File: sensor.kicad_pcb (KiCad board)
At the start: 2 copper layers, 18.4 x 42 mm, 13 parts, among them J1 Conn_01x06_Female, U2 TLV70019_SOT23-5, U3 TXB0106PWR, U4 PMW3360DM-T2QU

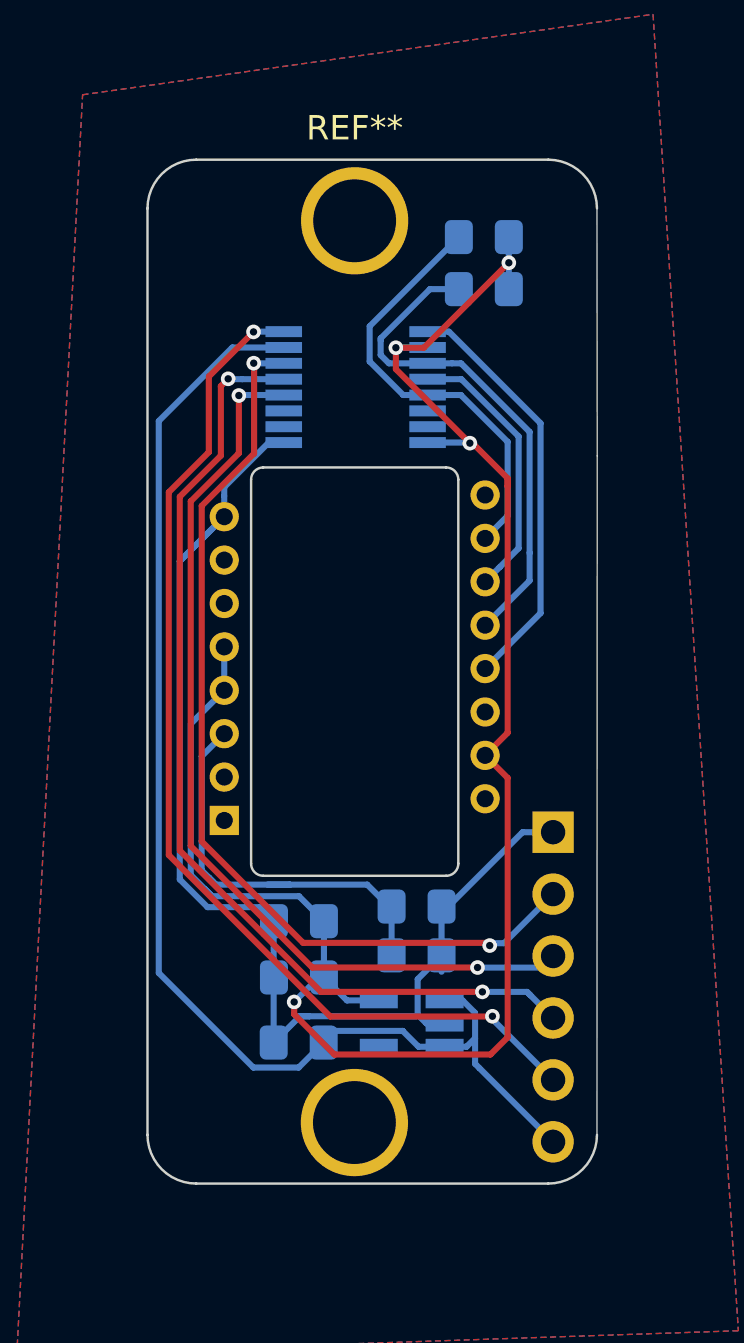
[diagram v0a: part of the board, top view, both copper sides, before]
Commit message: slightly bigger edge cuts for M3 holes
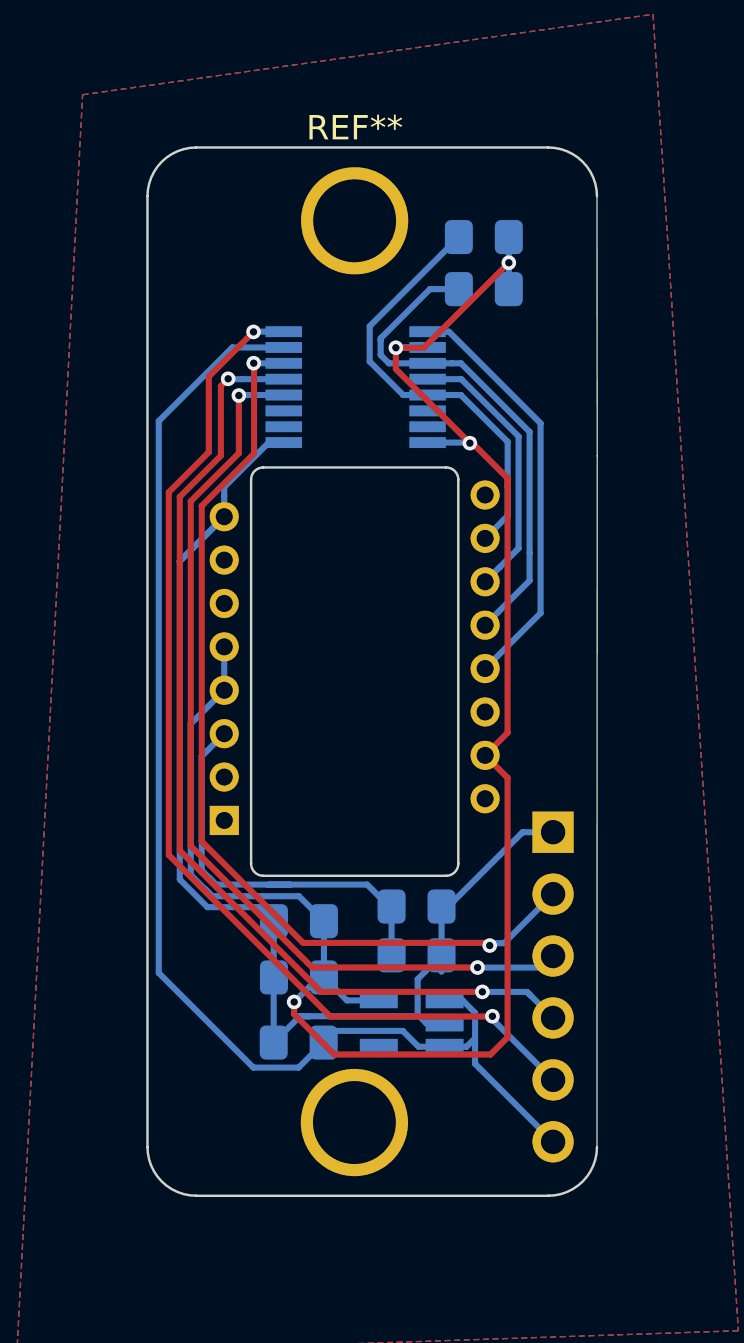
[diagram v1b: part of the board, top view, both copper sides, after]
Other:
- board size 18.4 x 42 mm -> 18.4 x 43 mm
- board text added: "rev 1.1"
- board text removed: "rev 1.0"
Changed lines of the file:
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@@
       (viasonmask false)
       (mode 1)
-      (useauxorigin false)
+      (useauxorigin true)
       (hpglpennumber 1)
       (hpglpenspeed 20)
@@
       (drillshape 0)
       (scaleselection 1)
-      (outputdirectory "../gerber/sensorPcb/")
+      (outputdirectory "gerber/")
     )
   )
@@
     (fp_line (start 1 -0.6) (end -1 -0.6) (layer "B.Fab") (width 0.1))
     (fp_line (start -1 -0.6) (end -1 0.6) (layer "B.Fab") (width 0.1))
-    (pad "1" smd roundrect (at -1.025 0) (locked) (size 1.15 1.4) (layers "B.Cu" "B.Paste" "B.Mask") (roundrect_rratio 0.217391)
+    (pad "1" smd roundrect (at -1.025 0) (locked) (size 1.15 1.4) (layers "B.Cu" "B.Paste" "B.Mask") (roundrect_rratio 0.2173913043478261)
       (net 12 "MISO") (pintype "passive"))
-    (pad "2" smd roundrect (at 1.025 0) (locked) (size 1.15 1.4) (layers "B.Cu" "B.Paste" "B.Mask") (roundrect_rratio 0.217391)
+    (pad "2" smd roundrect (at 1.025 0) (locked) (size 1.15 1.4) (layers "B.Cu" "B.Paste" "B.Mask") (roundrect_rratio 0.2173913043478261)
       (net 3 "VDD_1.9V") (pintype "passive"))
     (model "${KISYS3DMOD}/Resistor_SMD.3dshapes/R_0805_2012Metric.wrl"
@@
     (fp_line (start -1 0.6) (end 1 0.6) (layer "B.Fab") (width 0.1))
     (fp_line (start 1 0.6) (end 1 -0.6) (layer "B.Fab") (width 0.1))
-    (pad "1" smd roundrect (at -1.025 0) (locked) (size 1.15 1.4) (layers "B.Cu" "B.Paste" "B.Mask") (roundrect_rratio 0.217391)
+    (pad "1" smd roundrect (at -1.025 0) (locked) (size 1.15 1.4) (layers "B.Cu" "B.Paste" "B.Mask") (roundrect_rratio 0.2173913043478261)
       (net 10 "SCLK") (pintype "passive"))
-    (pad "2" smd roundrect (at 1.025 0) (locked) (size 1.15 1.4) (layers "B.Cu" "B.Paste" "B.Mask") (roundrect_rratio 0.217391)
+    (pad "2" smd roundrect (at 1.025 0) (locked) (size 1.15 1.4) (layers "B.Cu" "B.Paste" "B.Mask") (roundrect_rratio 0.2173913043478261)
       (net 3 "VDD_1.9V") (pintype "passive"))
     (model "${KISYS3DMOD}/Resistor_SMD.3dshapes/R_0805_2012Metric.wrl"
@@
     (fp_line (start 1 0.6) (end 1 -0.6) (layer "B.Fab") (width 0.1))
     (fp_line (start -1 0.6) (end 1 0.6) (layer "B.Fab") (width 0.1))
-    (pad "1" smd roundrect (at -1.025 0 180) (locked) (size 1.15 1.4) (layers "B.Cu" "B.Paste" "B.Mask") (roundrect_rratio 0.217391)
+    (pad "1" smd roundrect (at -1.025 0 180) (locked) (size 1.15 1.4) (layers "B.Cu" "B.Paste" "B.Mask") (roundrect_rratio 0.2173913043478261)
       (net 3 "VDD_1.9V") (pintype "passive"))
-    (pad "2" smd roundrect (at 1.025 0 180) (locked) (size 1.15 1.4) (layers "B.Cu" "B.Paste" "B.Mask") (roundrect_rratio 0.217391)
+    (pad "2" smd roundrect (at 1.025 0 180) (locked) (size 1.15 1.4) (layers "B.Cu" "B.Paste" "B.Mask") (roundrect_rratio 0.2173913043478261)
       (net 1 "GND") (pintype "passive"))
     (model "${KISYS3DMOD}/Capacitor_SMD.3dshapes/C_0805_2012Metric.wrl"
@@
     (fp_line (start 1 0.6) (end 1 -0.6) (layer "B.Fab") (width 0.1))
     (fp_line (start -1 -0.6) (end -1 0.6) (layer "B.Fab") (width 0.1))
-    (pad "1" smd roundrect (at -1.025 0 180) (locked) (size 1.15 1.4) (layers "B.Cu" "B.Paste" "B.Mask") (roundrect_rratio 0.217391)
+    (pad "1" smd roundrect (at -1.025 0 180) (locked) (size 1.15 1.4) (layers "B.Cu" "B.Paste" "B.Mask") (roundrect_rratio 0.2173913043478261)
       (net 2 "VDD_5V") (pintype "passive"))
-    (pad "2" smd roundrect (at 1.025 0 180) (locked) (size 1.15 1.4) (layers "B.Cu" "B.Paste" "B.Mask") (roundrect_rratio 0.217391)
+    (pad "2" smd roundrect (at 1.025 0 180) (locked) (size 1.15 1.4) (layers "B.Cu" "B.Paste" "B.Mask") (roundrect_rratio 0.2173913043478261)
       (net 1 "GND") (pintype "passive"))
     (model "${KISYS3DMOD}/Capacitor_SMD.3dshapes/C_0805_2012Metric.wrl"
@@
     (fp_line (start -1 -0.6) (end -1 0.6) (layer "B.Fab") (width 0.1))
     (fp_line (start 1 0.6) (end 1 -0.6) (layer "B.Fab") (width 0.1))
-    (pad "1" smd roundrect (at -1.025 0) (locked) (size 1.15 1.4) (layers "B.Cu" "B.Paste" "B.Mask") (roundrect_rratio 0.217391)
+    (pad "1" smd roundrect (at -1.025 0) (locked) (size 1.15 1.4) (layers "B.Cu" "B.Paste" "B.Mask") (roundrect_rratio 0.2173913043478261)
       (net 4 "Net-(C3-Pad1)"))
-    (pad "2" smd roundrect (at 1.025 0) (locked) (size 1.15 1.4) (layers "B.Cu" "B.Paste" "B.Mask") (roundrect_rratio 0.217391)
+    (pad "2" smd roundrect (at 1.025 0) (locked) (size 1.15 1.4) (layers "B.Cu" "B.Paste" "B.Mask") (roundrect_rratio 0.2173913043478261)
       (net 1 "GND"))
     (model "${KISYS3DMOD}/Capacitor_SMD.3dshapes/C_0805_2012Metric.wrl"
@@
     (fp_line (start 1 -0.6) (end -1 -0.6) (layer "B.Fab") (width 0.1))
     (fp_line (start -1 -0.6) (end -1 0.6) (layer "B.Fab") (width 0.1))
-    (pad "1" smd roundrect (at -1.025 0 180) (locked) (size 1.15 1.4) (layers "B.Cu" "B.Paste" "B.Mask") (roundrect_rratio 0.217391)
+    (pad "1" smd roundrect (at -1.025 0 180) (locked) (size 1.15 1.4) (layers "B.Cu" "B.Paste" "B.Mask") (roundrect_rratio 0.2173913043478261)
       (net 3 "VDD_1.9V") (pintype "passive"))
-    (pad "2" smd roundrect (at 1.025 0 180) (locked) (size 1.15 1.4) (layers "B.Cu" "B.Paste" "B.Mask") (roundrect_rratio 0.217391)
+    (pad "2" smd roundrect (at 1.025 0 180) (locked) (size 1.15 1.4) (layers "B.Cu" "B.Paste" "B.Mask") (roundrect_rratio 0.2173913043478261)
       (net 1 "GND") (pintype "passive"))
     (model "${KISYS3DMOD}/Resistor_SMD.3dshapes/R_0805_2012Metric.wrl"
@@
     (fp_line (start -1 0.6) (end 1 0.6) (layer "B.Fab") (width 0.1))
     (fp_line (start 1 0.6) (end 1 -0.6) (layer "B.Fab") (width 0.1))
-    (pad "1" smd roundrect (at -1.025 0) (locked) (size 1.15 1.4) (layers "B.Cu" "B.Paste" "B.Mask") (roundrect_rratio 0.217391)
+    (pad "1" smd roundrect (at -1.025 0) (locked) (size 1.15 1.4) (layers "B.Cu" "B.Paste" "B.Mask") (roundrect_rratio 0.2173913043478261)
       (net 4 "Net-(C3-Pad1)") (pintype "passive"))
-    (pad "2" smd roundrect (at 1.025 0) (locked) (size 1.15 1.4) (layers "B.Cu" "B.Paste" "B.Mask") (roundrect_rratio 0.217391)
+    (pad "2" smd roundrect (at 1.025 0) (locked) (size 1.15 1.4) (layers "B.Cu" "B.Paste" "B.Mask") (roundrect_rratio 0.2173913043478261)
       (net 1 "GND") (pintype "passive"))
     (model "${KISYS3DMOD}/Capacitor_SMD.3dshapes/C_0805_2012Metric.wrl"
@@
   (gr_line (start 77.812 119.038001) (end 85.312 119.038001) (layer "Edge.Cuts") (width 0.1))
   (gr_line (start 77.312 118.538001) (end 77.312 102.788001) (layer "Edge.Cuts") (width 0.1))
-  (gr_line (start 73.062 91.663) (end 73.062 129.663) (layer "Edge.Cuts") (width 0.1))
-  (gr_line (start 91.51 101.814214) (end 91.5 91.663) (layer "Edge.Cuts") (width 0.05))
-  (gr_arc (start 89.5 91.663) (end 91.5 91.663) (angle -90) (layer "Edge.Cuts") (width 0.1))
+  (gr_line (start 73.062 91.163) (end 73.062 130.163) (layer "Edge.Cuts") (width 0.1))
+  (gr_line (start 91.51 101.814214) (end 91.5 91.163) (layer "Edge.Cuts") (width 0.05))
+  (gr_arc (start 89.5 91.163) (end 91.5 91.163) (angle -90) (layer "Edge.Cuts") (width 0.1))
   (gr_line (start 77.812 102.288001) (end 85.312 102.288001) (layer "Edge.Cuts") (width 0.1))
   (gr_arc (start 77.812 118.538001) (end 77.312 118.538001) (angle -90) (layer "Edge.Cuts") (width 0.1))
-  (gr_arc (start 75.062 129.663) (end 73.062 129.663) (angle -90) (layer "Edge.Cuts") (width 0.1))
-  (gr_line (start 89.5 89.663) (end 75.062 89.663) (layer "Edge.Cuts") (width 0.1))
-  (gr_arc (start 89.500001 129.663001) (end 89.500002 131.663) (angle -90) (layer "Edge.Cuts") (width 0.1))
-  (gr_arc (start 75.062 91.663) (end 75.062 89.663) (angle -90) (layer "Edge.Cuts") (width 0.1))
+  (gr_arc (start 75.062 130.163) (end 73.062 130.163) (angle -90) (layer "Edge.Cuts") (width 0.1))
+  (gr_line (start 89.5 89.163) (end 75.062 89.163) (layer "Edge.Cuts") (width 0.1))
+  (gr_arc (start 89.500001 130.163001) (end 89.500002 132.163) (angle -90) (layer "Edge.Cuts") (width 0.1))
+  (gr_arc (start 75.062 91.163) (end 75.062 89.163) (angle -90) (layer "Edge.Cuts") (width 0.1))
   (gr_line (start 85.812 102.788001) (end 85.812 118.538001) (layer "Edge.Cuts") (width 0.1))
-  (gr_line (start 75.062 131.663) (end 89.500002 131.663) (layer "Edge.Cuts") (width 0.1))
+  (gr_line (start 75.062 132.163) (end 89.500002 132.163) (layer "Edge.Cuts") (width 0.1))
   (gr_arc (start 85.312 102.788001) (end 85.812 102.788001) (angle -90) (layer "Edge.Cuts") (width 0.1))
-  (gr_line (start 91.51 101.814214) (end 91.5 129.663) (layer "Edge.Cuts") (width 0.05))
+  (gr_line (start 91.51 101.814214) (end 91.5 130.163) (layer "Edge.Cuts") (width 0.05))
   (gr_arc (start 85.312 118.538001) (end 85.312 119.038001) (angle -90) (layer "Edge.Cuts") (width 0.1))
   (gr_arc (start 77.812 102.788001) (end 77.812 102.288001) (angle -90) (layer "Edge.Cuts") (width 0.1))
@@
     (effects (font (size 0.75 0.75) (thickness 0.1)) (justify mirror))
   )
-  (gr_text "rev 1.0" (at 88.3 90.9) (layer "B.SilkS")
+  (gr_text "rev 1.1" (at 88.3 90.9) (layer "B.SilkS")
     (effects (font (size 0.75 0.75) (thickness 0.1)) (justify mirror))
   )

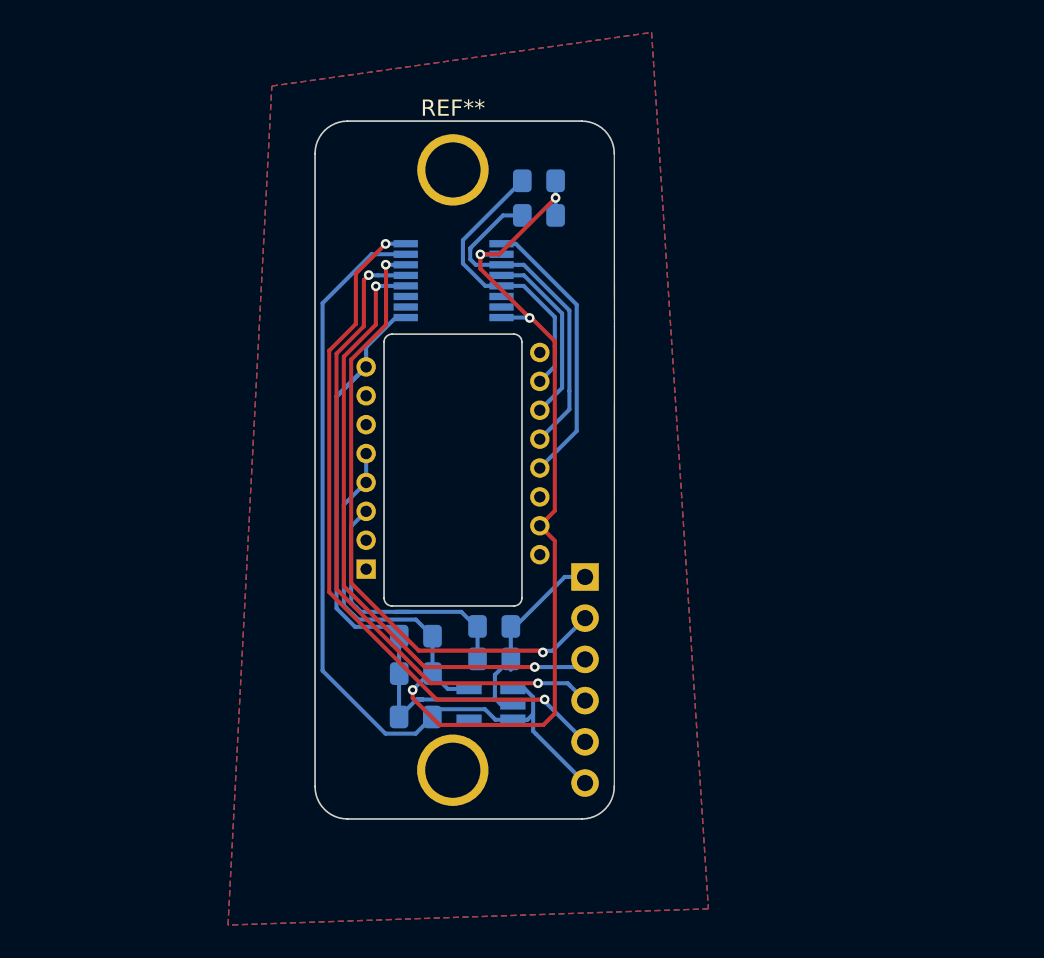
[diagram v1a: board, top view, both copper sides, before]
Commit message: screw clearance, edge cuts
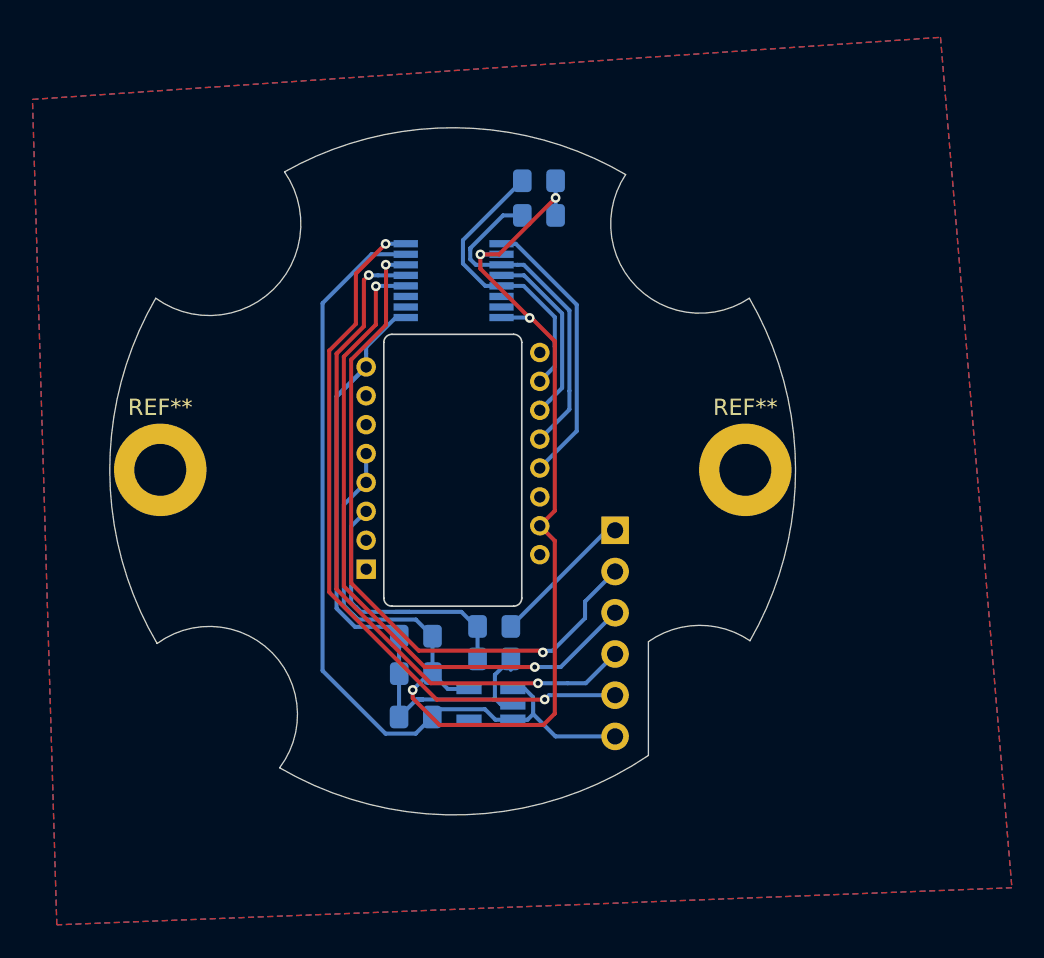
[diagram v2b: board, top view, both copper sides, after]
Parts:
- removed the REF** at (81.6, 92.2)
- added REF**: MountingHole_3.2mm_M3_ISO7380_Pad, MountingHole:MountingHole_3.2mm_M3_ISO7380_Pad, F.Cu at (63.5, 110.7)
- added REF**: MountingHole_3.2mm_M3_ISO7380_Pad, MountingHole:MountingHole_3.2mm_M3_ISO7380_Pad, F.Cu at (99.6, 110.7)
- moved J1 3.42 mm to (91.5, 114.4)
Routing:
- net MISO_I: track 38.8 -> 42.4 mm
- net SCLK_I: track 38.3 -> 41.3 mm
- net MOSI_I: track 40.8 -> 42.8 mm
- net GND: track 51.5 -> 52.6 mm
- net NCS_I: track 43.8 -> 44.7 mm
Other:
- board size 18.4 x 43 mm -> 42.3 x 42.3 mm
- board text added: "rev 1.2"
- board text removed: "rev 1.1"
